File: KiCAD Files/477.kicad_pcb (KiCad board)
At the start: 2 copper layers, 58 parts, among them IC1 W25N01GVSFIG, IC2 W25N01GVSFIG, IC3 W25N01GVSFIG, IC4 W25N01GVSFIG, IC5 AZ1117IH-3.3TRG1, IC6 USBLC6-2SC6, J1 BM06B-SRSS-TBT_LF__SN_, J2 6364372-2, J3 TSW-103-14-S-D, J4 TSW-103-14-S-D, J5 BM07B-SRSS-TB_LF__SN_, J6 BM09B-SRSS-TB_LF__SN_, U1 STM32H7A3RGTx, Y1 ABM8G-48.000MHZ-18-D2Y-T

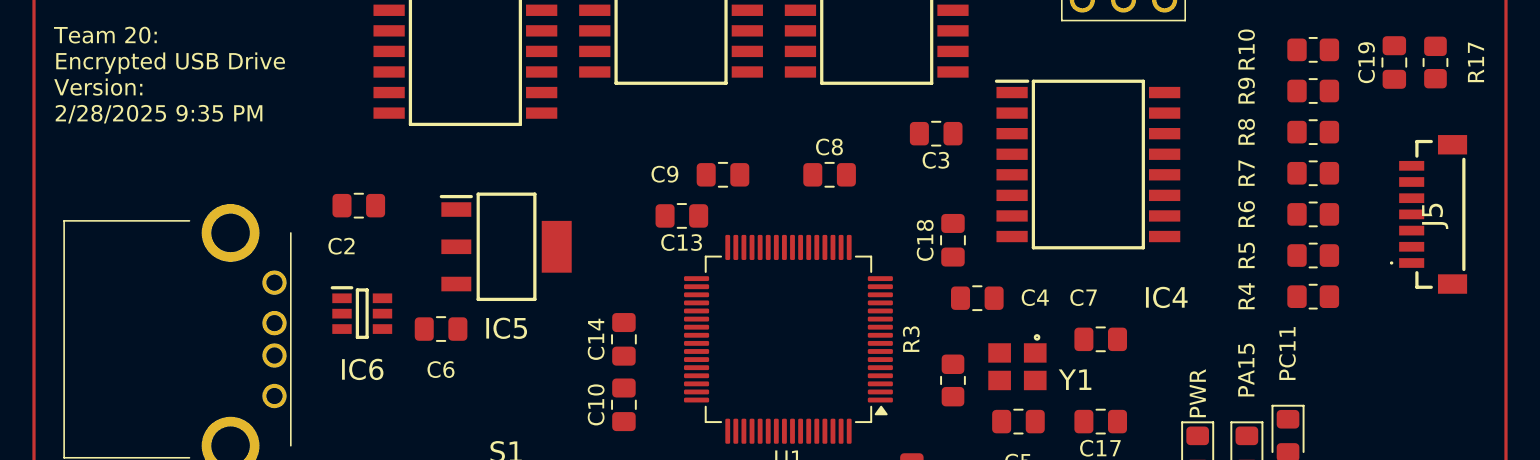
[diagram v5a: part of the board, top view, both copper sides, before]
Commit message: updated with 3d models
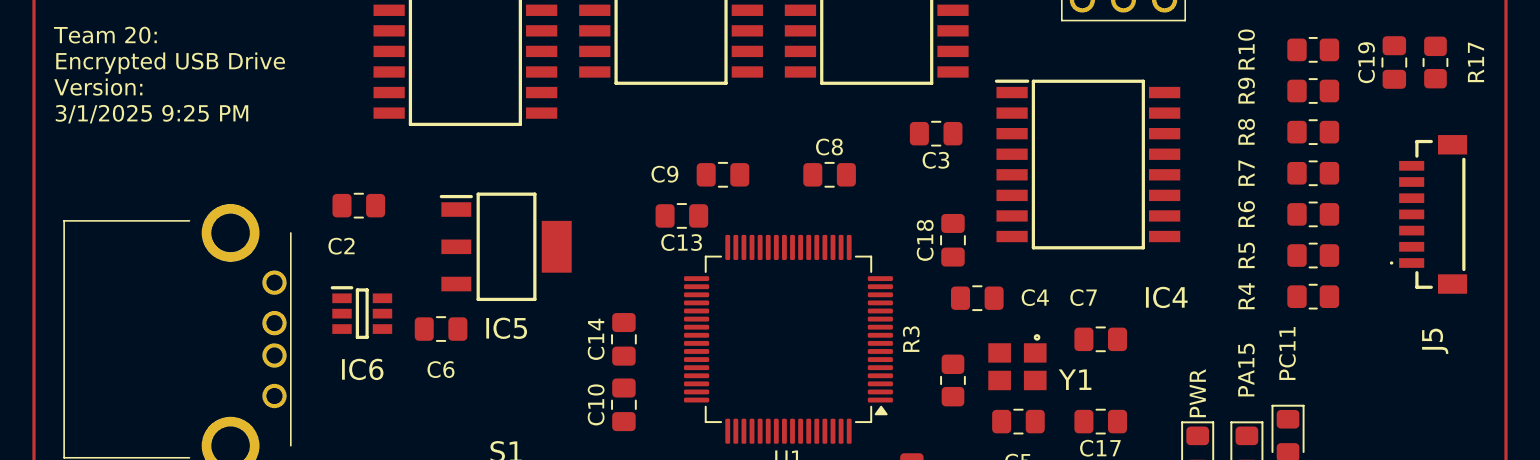
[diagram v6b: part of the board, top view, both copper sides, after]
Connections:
- net Net-(IC6-I/O1_1) renamed D-
- net Net-(IC6-I/O2_1) renamed D+
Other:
- board text added: "Team 20: Encrypted USB Drive Version: 3/1/2025 9:25 PM"
- board text removed: "Team 20: Encrypted USB Drive Version: 2/28/2025 9:35 PM"
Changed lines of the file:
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@@
 	(net 108 "unconnected-(J6-PadMP1)")
 	(net 109 "unconnected-(J6-Pad5)")
-	(net 110 "Net-(IC6-I{slash}O2_1)")
-	(net 111 "Net-(IC6-I{slash}O1_1)")
+	(net 110 "D+")
+	(net 111 "D-")
 	(footprint "Resistor_SMD:R_0805_2012Metric_Pad1.20x1.40mm_HandSolder"
 		(layer "F.Cu")
@@
 		)
 		(model "TSW-103-14-S-D.stp"
+			(hide yes)
 			(offset
 				(xyz 2.589999875 1.129999978 0.06999999925)
@@
 			)
 		)
+		(model "C:/Users/Jay62/Downloads/LIB_TSW-103-14-S-D/TSW-103-14-S-D/3D/TSW-103-14-S-D.stp"
+			(offset
+				(xyz 2.5 1.5 0)
+			)
+			(scale
+				(xyz 1 1 1)
+			)
+			(rotate
+				(xyz -90 0 0)
+			)
+		)
 	)
 	(footprint "Resistor_SMD:R_0805_2012Metric_Pad1.20x1.40mm_HandSolder"
@@
 			)
 		)
-		(property "Footprint" "SOIC127P1032X264-16N"
+		(property "Footprint" "CustomFootprints:SOIC127P1032X264-16N"
 			(at 0 0 0)
 			(layer "F.Fab")
@@
 		)
 		(model "W25N01GVSFIG.stp"
+			(hide yes)
+			(offset
+				(xyz 0 0 0)
+			)
+			(scale
+				(xyz 1 1 1)
+			)
+			(rotate
+				(xyz 0 0 0)
+			)
+		)
+		(model "C:/Users/Jay62/Downloads/LIB_W25N01GVSFIG/W25N01GVSFIG/3D/W25N01GVSFIG.stp"
 			(offset
 				(xyz 0 0 0)
@@
 		)
 		(model "TSW-103-14-S-D.stp"
+			(hide yes)
 			(offset
 				(xyz 2.589999875 1.129999978 0.06999999925)
@@
 			)
 		)
+		(model "C:/Users/Jay62/Downloads/LIB_TSW-103-14-S-D/TSW-103-14-S-D/3D/TSW-103-14-S-D.stp"
+			(offset
+				(xyz 2.5 1.5 0)
+			)
+			(scale
+				(xyz 1 1 1)
+			)
+			(rotate
+				(xyz -90 0 0)
+			)
+		)
 	)
 	(footprint "CustomFootprints:63643722"
@@
 			)
 		)
-		(property "Footprint" "63643722"
+		(property "Footprint" "CustomFootprints:63643722"
 			(at 0 0 90)
 			(layer "F.Fab")
@@
 			(layers "*.Cu" "*.Mask")
 			(remove_unused_layers no)
-			(net 111 "Net-(IC6-I{slash}O1_1)")
+			(net 111 "D-")
 			(pinfunction "2")
 			(pintype "passive")
@@
 			(layers "*.Cu" "*.Mask")
 			(remove_unused_layers no)
-			(net 110 "Net-(IC6-I{slash}O2_1)")
+			(net 110 "D+")
 			(pinfunction "3")
 			(pintype "passive")
@@
 			)
 		)
+		(model "C:/Users/Jay62/Downloads/LIB_6364372-2/6364372-2/3D/6364372-2.stp"
+			(offset
+				(xyz 3.5 -13 3.9)
+			)
+			(scale
+				(xyz 1 1 1)
+			)
+			(rotate
+				(xyz -90 0 0)
+			)
+		)
 	)
 	(footprint "Resistor_SMD:R_0805_2012Metric_Pad1.20x1.40mm_HandSolder"
@@
 			)
 		)
-		(property "Footprint" "SOIC127P1032X264-16N"
+		(property "Footprint" "CustomFootprints:SOIC127P1032X264-16N"
 			(at 0 0 0)
 			(layer "F.Fab")
@@
 		)
 		(model "W25N01GVSFIG.stp"
+			(hide yes)
+			(offset
+				(xyz 0 0 0)
+			)
+			(scale
+				(xyz 1 1 1)
+			)
+			(rotate
+				(xyz 0 0 0)
+			)
+		)
+		(model "C:/Users/Jay62/Downloads/LIB_W25N01GVSFIG/W25N01GVSFIG/3D/W25N01GVSFIG.stp"
 			(offset
 				(xyz 0 0 0)
@@
 			)
 		)
-		(property "Footprint" "BM06BSRSSTBTLFSN"
+		(property "Footprint" "CustomFootprints:BM06BSRSSTBTLFSN"
 			(at 0 0 0)
 			(layer "F.Fab")
@@
 			)
 		)
+		(model "C:/Users/Jay62/Downloads/LIB_BM06B-SRSS-TBT_LF__SN_/BM06B-SRSS-TBT_LF__SN_/3D/BM06B-SRSS-TBT_LF__SN_.stp"
+			(offset
+				(xyz 0 0 0)
+			)
+			(scale
+				(xyz 1 1 1)
+			)
+			(rotate
+				(xyz 0 0 0)
+			)
+		)
 	)
 	(footprint "Resistor_SMD:R_0805_2012Metric_Pad1.20x1.40mm_HandSolder"
@@
 			)
 		)
-		(property "Footprint" "SOIC127P1032X264-16N"
+		(property "Footprint" "CustomFootprints:SOIC127P1032X264-16N"
 			(at 0 0 0)
 			(layer "F.Fab")
@@
 		)
 		(model "W25N01GVSFIG.stp"
+			(hide yes)
+			(offset
+				(xyz 0 0 0)
+			)
+			(scale
+				(xyz 1 1 1)
+			)
+			(rotate
+				(xyz 0 0 0)
+			)
+		)
+		(model "C:/Users/Jay62/Downloads/LIB_W25N01GVSFIG/W25N01GVSFIG/3D/W25N01GVSFIG.stp"
 			(offset
 				(xyz 0 0 0)
@@
 			)
 		)
-		(property "Footprint" "ABM8G"
+		(property "Footprint" "CustomFootprints:ABM8G"
 			(at 0 0 0)
 			(layer "F.Fab")
@@
 		)
 		(model "ABM8G-48.000MHZ-18-D2Y-T.stp"
+			(hide yes)
 			(offset
 				(xyz 0 -0.07999999701 0.009999999626)
@@
 			)
 		)
+		(model "C:/Users/Jay62/Downloads/LIB_ABM8G-48.000MHZ-18-D2Y-T/ABM8G-48.000MHZ-18-D2Y-T/3D/ABM8G-48.000MHZ-18-D2Y-T.stp"
+			(offset
+				(xyz 0 0 0)
+			)
+			(scale
+				(xyz 1 1 1)
+			)
+			(rotate
+				(xyz -90 0 0)
+			)
+		)
 	)
 	(footprint "Capacitor_SMD:C_0805_2012Metric_Pad1.18x1.45mm_HandSolder"
@@
 			)
 		)
-		(property "Footprint" "SOT95P280X145-6N"
+		(property "Footprint" "CustomFootprints:SOT95P280X145-6N"
 			(at 0 0 0)
 			(layer "F.Fab")
@@
 			(size 0.6 1.2)
 			(layers "F.Cu" "F.Paste" "F.Mask")
-			(net 111 "Net-(IC6-I{slash}O1_1)")
+			(net 111 "D-")
 			(pinfunction "I/O1_1")
 			(pintype "passive")
@@
 			(size 0.6 1.2)
 			(layers "F.Cu" "F.Paste" "F.Mask")
-			(net 110 "Net-(IC6-I{slash}O2_1)")
+			(net 110 "D+")
 			(pinfunction "I/O2_1")
 			(pintype "passive")
@@
 		)
 		(model "USBLC6-2SC6.stp"
+			(hide yes)
+			(offset
+				(xyz 0 0 0)
+			)
+			(scale
+				(xyz 1 1 1)
+			)
+			(rotate
+				(xyz 0 0 0)
+			)
+		)
+		(model "C:/Users/Jay62/Downloads/LIB_USBLC6-2SC6/USBLC6-2SC6/3D/USBLC6-2SC6.stp"
 			(offset
 				(xyz 0 0 0)
@@
 			)
 		)
-		(property "Footprint" "SOT230P700X180-4N"
+		(property "Footprint" "CustomFootprints:SOT230P700X180-4N"
 			(at 0 0 0)
 			(layer "F.Fab")
@@
 			)
 		)
+		(model "C:/Users/Jay62/Downloads/LIB_AZ1117IH-3.3TRG1/AZ1117IH-3.3TRG1/3D/AZ1117IH-3.3TRG1.stp"
+			(offset
+				(xyz 0 0 0)
+			)
+			(scale
+				(xyz 1 1 1)
+			)
+			(rotate
+				(xyz 0 0 0)
+			)
+		)
 	)
 	(footprint "CustomFootprints:BM07BSRSSTBLFSN"
@@
 		(tags "Connector")
 		(property "Reference" "J5"
-			(at 0 -0.449 90)
+			(at -7.715 -0.449 90)
 			(layer "F.SilkS")
 			(effects
@@
 			)
 		)
-		(property "Footprint" "BM07BSRSSTBLFSN"
+		(property "Footprint" "CustomFootprints:BM07BSRSSTBLFSN"
 			(at 0 0 90)
 			(layer "F.Fab")
@@
 			(layer "F.Fab")
 		)
-		(fp_text user "${REFERENCE}"
-			(at 0 -0.449 90)
-			(layer "F.Fab")
-			(effects
-				(font
-					(size 1.27 1.27)
-					(thickness 0.254)
-				)
-			)
-		)
 		(pad "1" smd rect
 			(at -3 -1.774 90)
@@
 			)
 		)
+		(model "C:/Users/Jay62/Downloads/LIB_BM07B-SRSS-TB_LF__SN_/BM07B-SRSS-TB_LF__SN_/3D/BM07B-SRSS-TB_LF__SN_.stp"
+			(offset
+				(xyz 0 0 0)
+			)
+			(scale
+				(xyz 1 1 1)
+			)
+			(rotate
+				(xyz 0 0 0)
+			)
+		)
 	)
 	(footprint "Capacitor_SMD:C_0805_2012Metric_Pad1.18x1.45mm_HandSolder"
@@
 			)
 		)
-		(property "Footprint" "SOIC127P1032X264-16N"
+		(property "Footprint" "CustomFootprints:SOIC127P1032X264-16N"
 			(at 0 0 0)
 			(layer "F.Fab")
@@
 		)
 		(model "W25N01GVSFIG.stp"
+			(hide yes)
+			(offset
+				(xyz 0 0 0)
+			)
+			(scale
+				(xyz 1 1 1)
+			)
+			(rotate
+				(xyz 0 0 0)
+			)
+		)
+		(model "C:/Users/Jay62/Downloads/LIB_W25N01GVSFIG/W25N01GVSFIG/3D/W25N01GVSFIG.stp"
 			(offset
 				(xyz 0 0 0)
@@
 			(layer "F.CrtYd")
 		)
+		(fp_text user "${REFERENCE}"
+			(at 0 0 0)
+			(layer "F.Fab")
+			(effects
+				(font
+					(size 1 1)
+					(thickness 0.15)
+				)
+			)
+		)
 		(pad "" np_thru_hole circle
 			(at 0 0)
@@
 			)
 		)
+		(model "C:/Users/Jay62/Downloads/LIB_222AMVBAR/222AMVBAR/3D/222AMVBAR.stp"
+			(offset
+				(xyz 0 0 0)
+			)
+			(scale
+				(xyz 1 1 1)
+			)
+			(rotate
+				(xyz 0 0 0)
+			)
+		)
 	)
 	(footprint "Capacitor_SMD:C_0805_2012Metric_Pad1.18x1.45mm_HandSolder"
@@
 			)
 		)
-		(property "Footprint" "BM09BSRSSTBLFSN"
+		(property "Footprint" "CustomFootprints:BM09BSRSSTBLFSN"
 			(at 0 0 0)
 			(layer "F.Fab")
@@
 			)
 		)
+		(model "C:/Users/Jay62/Downloads/LIB_BM09B-SRSS-TB_LF__SN_/BM09B-SRSS-TB_LF__SN_/3D/BM09B-SRSS-TB_LF__SN_.stp"
+			(offset
+				(xyz 0 0 0)
+			)
+			(scale
+				(xyz 1 1 1)
+			)
+			(rotate
+				(xyz 0 0 0)
+			)
+		)
 	)
 	(footprint "Capacitor_SMD:C_0805_2012Metric_Pad1.18x1.45mm_HandSolder"
@@
 		)
 	)
-	(gr_text "Team 20: \nEncrypted USB Drive\nVersion: \n2/28/2025 9:35 PM\n"
+	(gr_text "Team 20: \nEncrypted USB Drive\nVersion: \n3/1/2025 9:25 PM\n"
 		(at 111.665 93.345 0)
 		(layer "F.SilkS")

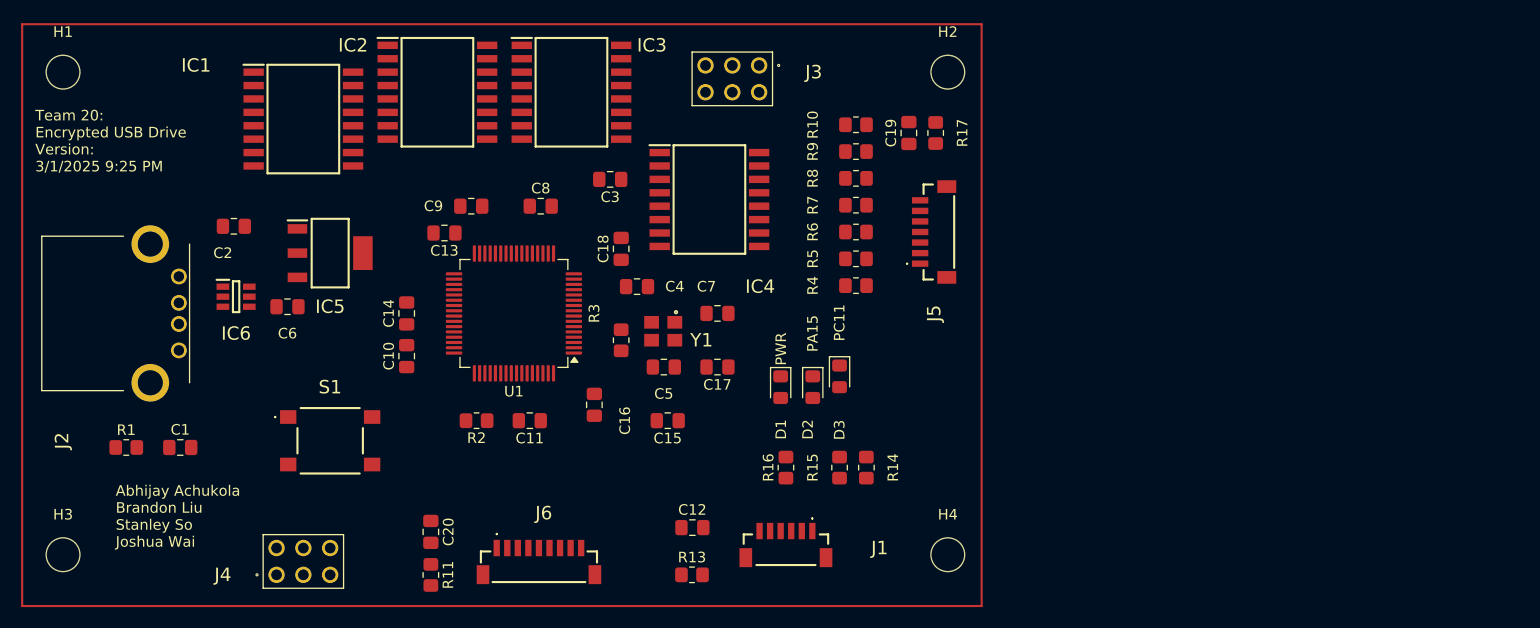
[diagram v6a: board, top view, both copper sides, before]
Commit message: added testing points
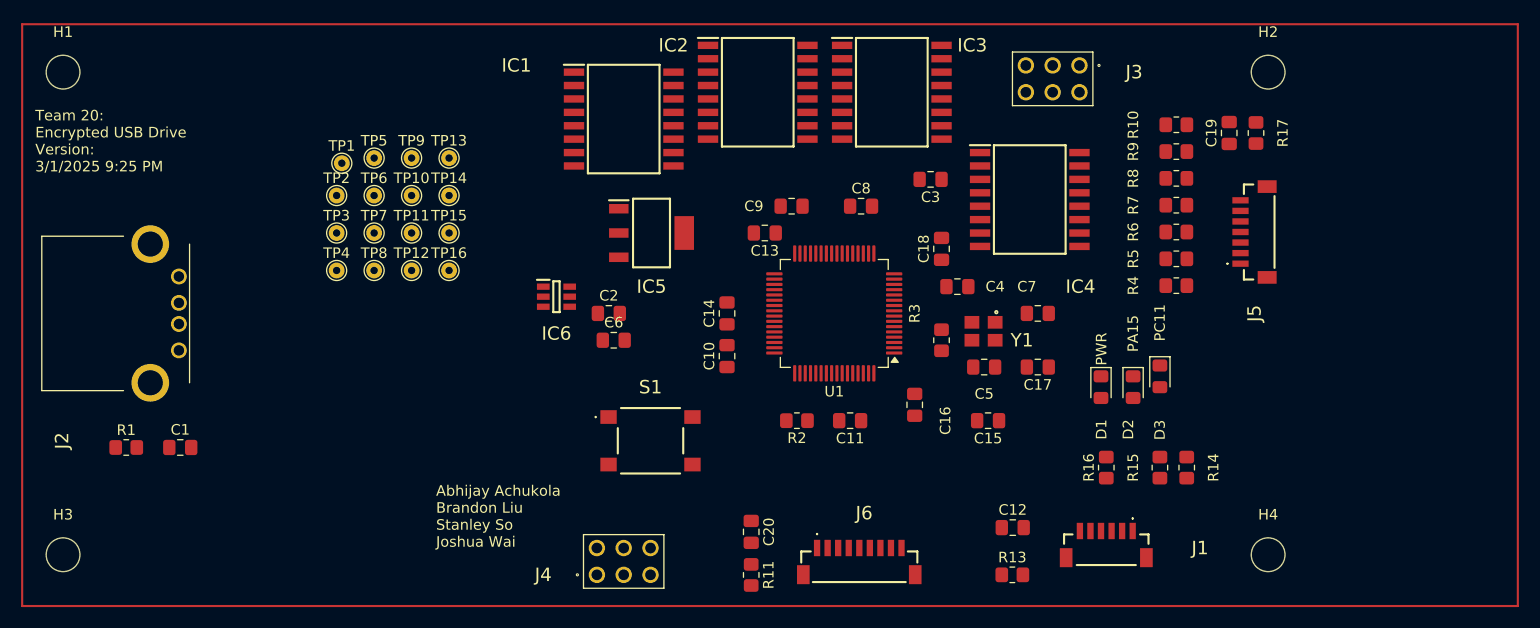
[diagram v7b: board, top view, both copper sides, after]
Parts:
- added TP1: TestPoint, TestPoint:TestPoint_THTPad_D1.5mm_Drill0.7mm, F.Cu at (140.7, 92.5)
- added TP10: TestPoint, TestPoint:TestPoint_THTPad_D1.5mm_Drill0.7mm, F.Cu at (147.3, 95.5)
- added TP11: TestPoint, TestPoint:TestPoint_THTPad_D1.5mm_Drill0.7mm, F.Cu at (147.3, 99.1)
- added TP12: TestPoint, TestPoint:TestPoint_THTPad_D1.5mm_Drill0.7mm, F.Cu at (147.3, 102.6)
- added TP13: TestPoint, TestPoint:TestPoint_THTPad_D1.5mm_Drill0.7mm, F.Cu at (150.9, 92.0)
- added TP14: TestPoint, TestPoint:TestPoint_THTPad_D1.5mm_Drill0.7mm, F.Cu at (150.9, 95.5)
- added TP15: TestPoint, TestPoint:TestPoint_THTPad_D1.5mm_Drill0.7mm, F.Cu at (150.9, 99.1)
- added TP16: TestPoint, TestPoint:TestPoint_THTPad_D1.5mm_Drill0.7mm, F.Cu at (150.9, 102.6)
- added TP2: TestPoint, TestPoint:TestPoint_THTPad_D1.5mm_Drill0.7mm, F.Cu at (140.2, 95.5)
- added TP3: TestPoint, TestPoint:TestPoint_THTPad_D1.5mm_Drill0.7mm, F.Cu at (140.2, 99.1)
- added TP4: TestPoint, TestPoint:TestPoint_THTPad_D1.5mm_Drill0.7mm, F.Cu at (140.2, 102.6)
- added TP5: TestPoint, TestPoint:TestPoint_THTPad_D1.5mm_Drill0.7mm, F.Cu at (143.8, 92.0)
- added TP6: TestPoint, TestPoint:TestPoint_THTPad_D1.5mm_Drill0.7mm, F.Cu at (143.8, 95.5)
- added TP7: TestPoint, TestPoint:TestPoint_THTPad_D1.5mm_Drill0.7mm, F.Cu at (143.8, 99.1)
- added TP8: TestPoint, TestPoint:TestPoint_THTPad_D1.5mm_Drill0.7mm, F.Cu at (143.8, 102.6)
- added TP9: TestPoint, TestPoint:TestPoint_THTPad_D1.5mm_Drill0.7mm, F.Cu at (147.3, 92.0)
- moved C2 36.5 mm to (166.0, 106.7)
- moved C6 31.1 mm to (166.5, 109.2)
- moved IC5 30.5 mm to (170.1, 99.1)
- moved C10 30.4 mm to (177.2, 110.7)
- moved C14 30.4 mm to (177.2, 106.7)
- moved C16 30.4 mm to (195.0, 115.3)
- moved C3 30.4 mm to (196.5, 94.0)
- moved D2 30.4 mm to (215.7, 113.7)
- moved IC2 30.4 mm to (180.1, 85.7)
- moved J6 30.4 mm to (189.7, 130.7)
- moved R10 30.4 mm to (219.8, 88.8)
- moved R13 30.4 mm to (204.2, 131.4)
- moved R4 30.4 mm to (219.8, 104.0)
- moved R5 30.4 mm to (219.8, 101.5)
- moved R6 30.4 mm to (219.8, 99.0)
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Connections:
- J4 pad 2: PB4/KeyC1 -> GND
- R10 pad 1: PB6/KeyC3 -> PB8/KeyC3
- R15 pad 2: PA15/Debug -> PA9/Debug
- R7 pad 1: PB3/KeyR4 -> PB5/KeyR4
- R8 pad 1: PB4/KeyC1 -> PB6/KeyC1
- R9 pad 2: PB5/KeyC2 -> PB7/KeyC2
- U1 pad 41: unconnected-(U1-PA9-Pad41) -> PA9/Debug
- U1 pad 45: unconnected-(U1-PA13-Pad45) -> PA13/JTMS/SWDIO
- U1 pad 49: unconnected-(U1-PA14-Pad49) -> PA14/JTCK/SWCLK
- U1 pad 50: PA15/Debug -> PA14/JTCK/SWCLK
- U1 pad 55: PB3/KeyR4 -> PB3/JTDO
- U1 pad 56: PB4/KeyC1 -> PB4/nJTRST
- U1 pad 57: PB5/KeyC2 -> PB5/KeyR4
- U1 pad 58: PB6/KeyC3 -> PB6/KeyC1
- U1 pad 59: unconnected-(U1-PB7-Pad59) -> PB7/KeyC2
- U1 pad 61: unconnected-(U1-PB8-Pad61) -> PB8/KeyC3
